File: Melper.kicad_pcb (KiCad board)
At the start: 2 copper layers, 160 x 60 mm, 41 parts, among them J1 Conn_01x02, J2 Conn_02x08_Odd_Even, J3 Conn_02x08_Odd_Even, J4 Conn_02x08_Odd_Even, J5 Conn_02x08_Odd_Even, J6 Conn_02x08_Odd_Even, U1 LM7805_TO220, U2 cui

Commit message: Version 2.1
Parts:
- removed C10, C11, C12, C13, C14, C15, C16, C17, C18, C19, C20, C21, C8, C9: .1uF, Capacitor_THT:C_Disc_D4.3mm_W1.9mm_P5.00mm
- C1: value .33uF -> 10uF; footprint Capacitor_THT:C_Disc_D4.3mm_W1.9mm_P5.00mm -> Capacitor_THT:CP_Radial_D8.0mm_P5.00mm
- C2: footprint Capacitor_THT:CP_Radial_Tantal_D5.0mm_P5.00mm -> Capacitor_THT:CP_Radial_D8.0mm_P5.00mm
- C5, C7: value .1uF -> 10uF; footprint Capacitor_THT:C_Disc_D4.3mm_W1.9mm_P5.00mm -> Capacitor_THT:CP_Radial_D8.0mm_P5.00mm
- C6: value 22uF -> 10uF; footprint Capacitor_THT:CP_Radial_Tantal_D6.0mm_P5.00mm -> Capacitor_THT:CP_Radial_D8.0mm_P5.00mm
- R1, R3: value 1K -> 10K
- R2: value 1K -> 4.7K
- U1: footprint Package_TO_SOT_THT:TO-220-3_Vertical -> Package_TO_SOT_THT:TO-220-3_Horizontal_TabDown
- U2: value cui -> VXO78012-1000
- moved J6 123.8 mm to (192.5, 88.3), turned to 180 degrees
- moved J2 89.2 mm to (72.5, 88.3), turned to 180 degrees
- moved U1 40.2 mm to (51.0, 47.8), turned to -90 degrees
- moved C4 38.6 mm to (45.1, 52.9), turned to -90 degrees
- moved C1 34.8 mm to (45.1, 47.8), turned to 90 degrees
- moved J5 32.7 mm to (162.5, 88.3), turned to 180 degrees
- moved C5 23.5 mm to (101.5, 43.9), turned to -90 degrees
- moved J3 18.0 mm to (102.5, 88.3), turned to 180 degrees
- moved J4 18.0 mm to (132.5, 88.3), turned to 180 degrees
- moved C6 16.4 mm to (101.5, 59.0), turned to 90 degrees
- moved C3 16.0 mm to (77.6, 47.8)
- moved L1 16.0 mm to (77.6, 52.8)
- moved U2 15.8 mm to (89.4, 52.8)
- moved C7 14.9 mm to (51.4, 78.1), turned to 90 degrees
- moved C2 14.4 mm to (88.0, 44.8), turned to 0 degrees
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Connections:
- C5 pad 1: -12V -> GND
- C5 pad 2: GND -> -12V
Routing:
- net +12V: track 0.00 -> 237.3 mm, vias 0 -> 2
- net -12V: track 185.7 -> 217.5 mm, vias 0 -> 2
- net Net-(D2-Pad2): track 9.13 -> 11.5 mm
- net Net-(D3-Pad2): track 6.44 -> 7.79 mm
- added copper zone on F.Cu, net GND
- removed copper zone on F.Cu, net +12V
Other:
- board text added: "-12V"
- board text added: "S/N 2.1."
- board text added: "v2.1"
- board text removed: "S/N 1.1."
- board text removed: "v1.1"

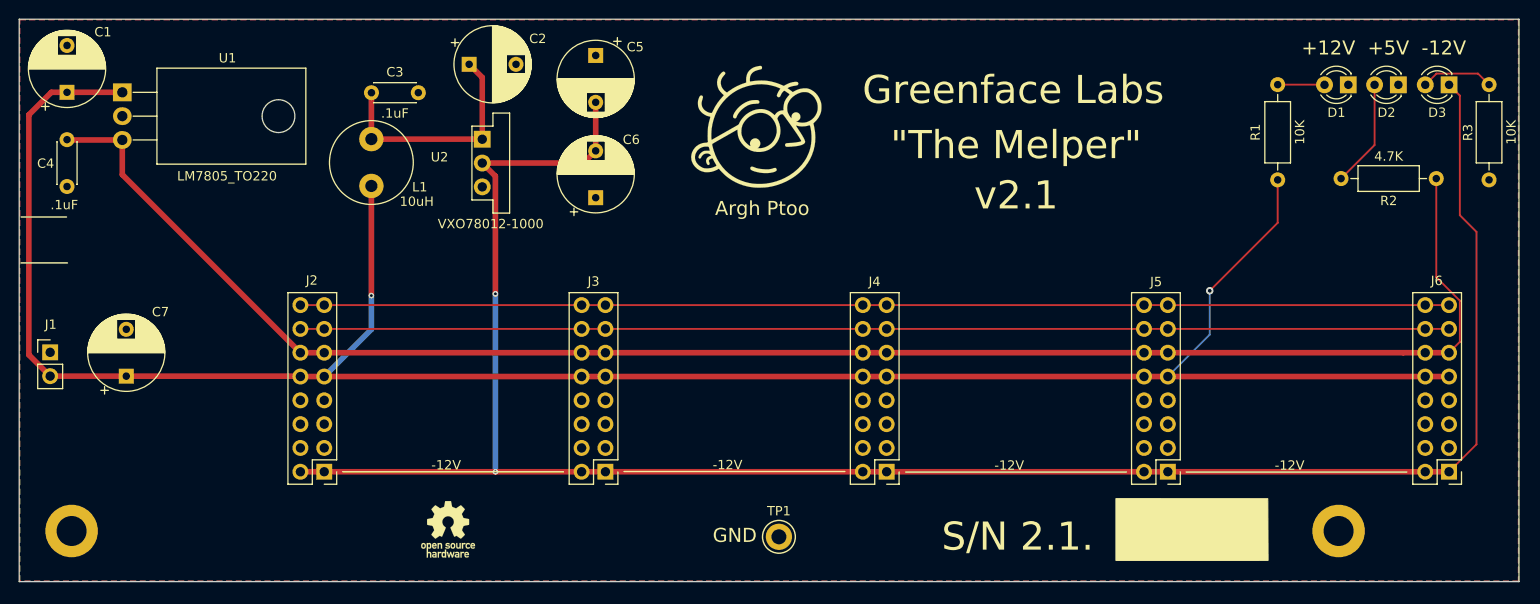
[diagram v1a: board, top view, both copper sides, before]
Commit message: Version 3
Adds 6th power connector.
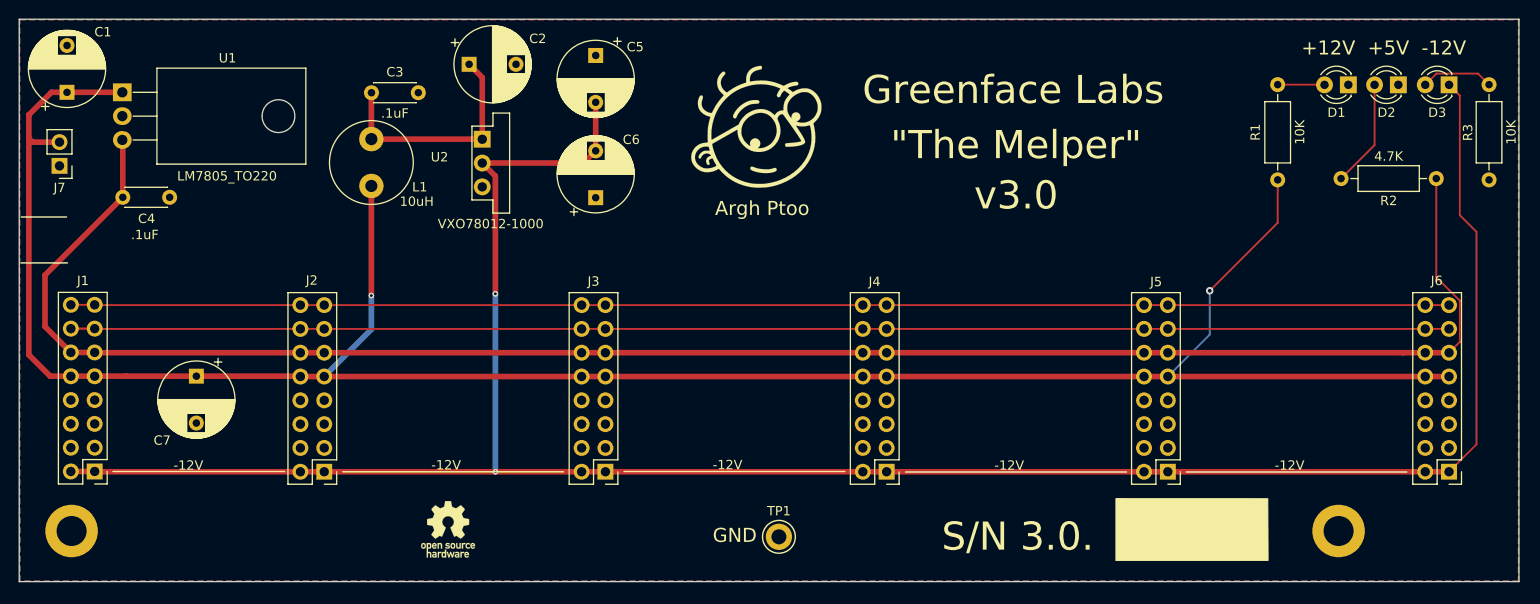
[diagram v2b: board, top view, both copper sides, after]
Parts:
- added J7: Conn_01x02, Connector_PinHeader_2.54mm:PinHeader_1x02_P2.54mm_Vertical, F.Cu at (44.3, 55.6)
- J1: value Conn_01x02 -> Conn_02x08_Odd_Even; footprint Connector_PinHeader_2.54mm:PinHeader_1x02_P2.54mm_Vertical -> Connector_PinHeader_2.54mm:PinHeader_2x08_P2.54mm_Vertical
- moved J1 13.6 mm to (48.0, 88.2), turned to 180 degrees
- moved C4 8.56 mm to (51.0, 59.0), turned to 0 degrees
- moved C7 7.48 mm to (58.9, 78.1), turned to -90 degrees
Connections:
- J1 pad 1: GND -> -12V
- J1 pad 2: +12V -> -12V
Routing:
- net CV: track 122.5 -> 147.0 mm
- net -12V: track 217.5 -> 242.0 mm
- net GATE: track 122.5 -> 147.0 mm
- net +5V: track 179.1 -> 194.4 mm
- net +12V: track 237.3 -> 240.7 mm
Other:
- board text added: "S/N 3.0."
- board text added: "v3.0"
- board text removed: "S/N 2.1."
- board text removed: "v2.1"

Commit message: Rev 3.2
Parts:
- added TP2: TestPoint, TestPoint:TestPoint_Pad_D2.0mm, F.Cu at (94.1, 95.2)
- added TP3: TestPoint, TestPoint:TestPoint_Pad_D2.0mm, F.Cu at (110.0, 95.2)
- added TP4: TestPoint, TestPoint:TestPoint_Pad_D2.0mm, F.Cu at (102.5, 95.2)
- moved H1 10.0 mm to (55.6, 95.6)
- moved GR2 5.00 mm to (80.8, 94.4)
- moved H2 1.00 mm to (180.8, 95.6)
- moved J7 0.98 mm to (44.1, 56.6), turned to 0 degrees
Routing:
- net +5V: track 194.4 -> 217.2 mm, vias 0 -> 1
- net +12V: track 240.7 -> 259.9 mm, vias 2 -> 3
- net -12V: track 242.0 -> 249.0 mm, vias 2 -> 3
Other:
- board text added: "+12"
- board text added: "+12V"
- board text added: "+5V"
- board text added: "S/N 3.2."
- board text added: "v3.2"
- board text removed: "S/N 3.0."
- board text removed: "v3.0"

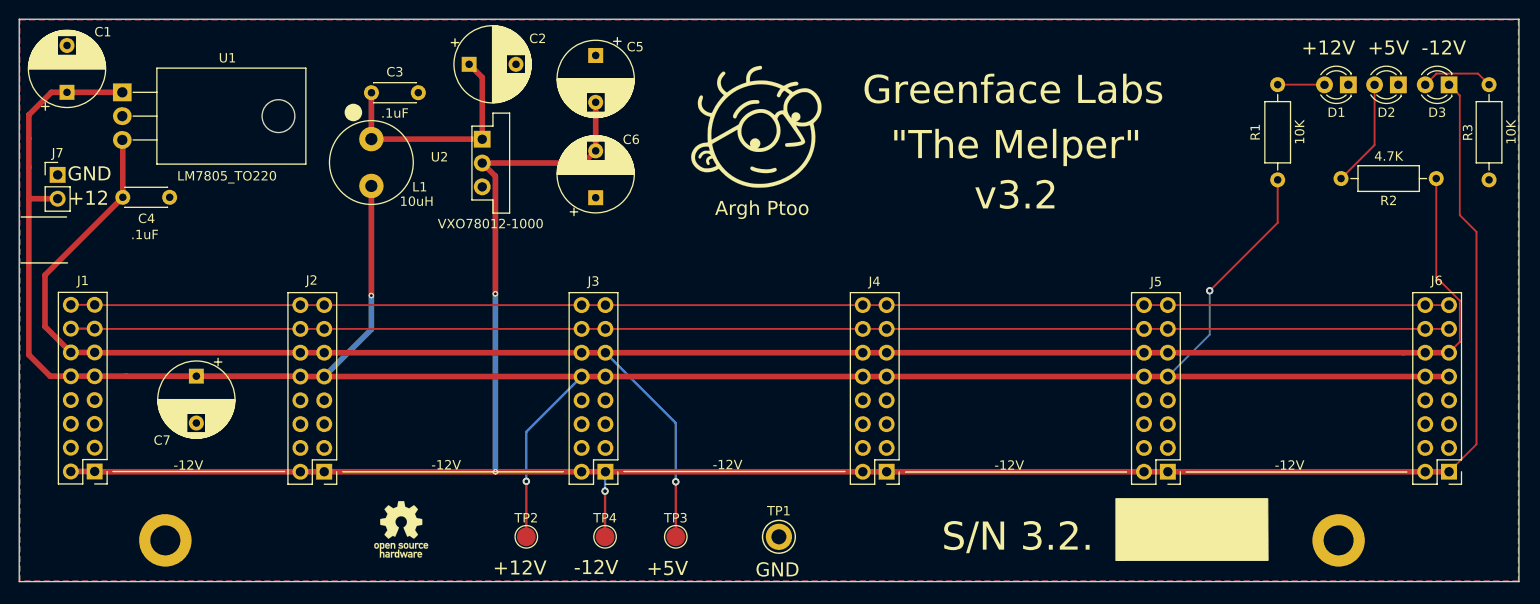
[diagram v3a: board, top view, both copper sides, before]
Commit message: Revision 3.5
Changes negative regulator.
Adds support for JLC build.
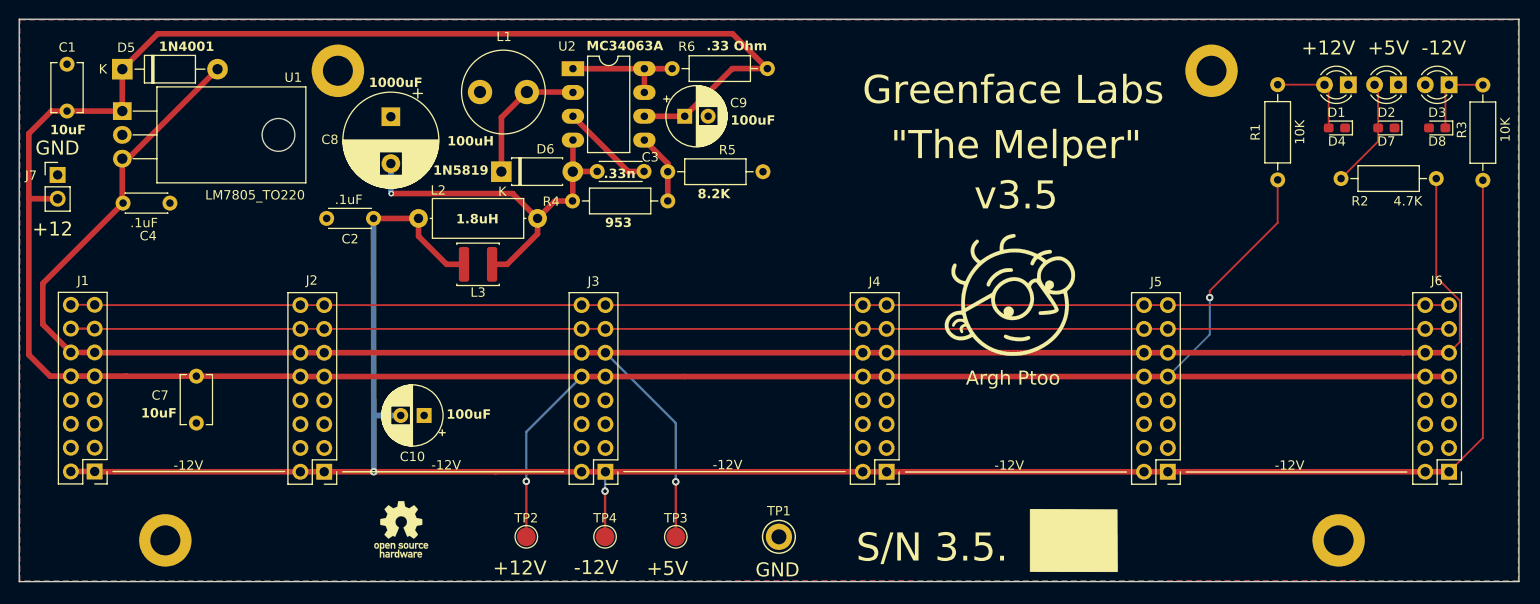
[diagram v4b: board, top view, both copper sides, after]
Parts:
- removed C5, C6: 10uF, Capacitor_THT:CP_Radial_D8.0mm_P5.00mm
- added C10: 100uF, Capacitor_THT:CP_Radial_D6.3mm_P2.50mm, F.Cu at (83.2, 82.3)
- added C8: 1000uF, Capacitor_THT:CP_Radial_D10.0mm_P5.00mm, F.Cu at (79.7, 50.4)
- added C9: 100uF, Capacitor_THT:CP_Radial_D6.3mm_P2.50mm, F.Cu at (111.0, 50.4)
- added D4: Red SMT LED, LED_SMD:LED_0603_1608Metric_Pad1.05x0.95mm_HandSolder, F.Cu at (180.6, 51.6)
- added D5: 1N4001, Diode_THT:D_DO-41_SOD81_P10.16mm_Horizontal, F.Cu at (51.0, 45.3)
- added D6: 1N5819, Diode_THT:D_DO-41_SOD81_P7.62mm_Horizontal, F.Cu at (91.4, 56.3)
- added D7: Yellow LED, LED_SMD:LED_0603_1608Metric_Pad1.05x0.95mm_HandSolder, F.Cu at (185.8, 51.6)
- added D8: Blue SMT LED, LED_SMD:LED_0603_1608Metric_Pad1.05x0.95mm_HandSolder, F.Cu at (191.3, 51.6)
- added H3: MountingHole_Pad, MountingHole:MountingHole_3.2mm_M3_DIN965_Pad, F.Cu at (74.0, 45.5)
- added H4: MountingHole_Pad, MountingHole:MountingHole_3.2mm_M3_DIN965_Pad, F.Cu at (167.2, 45.5)
- added L2: 1.8uH, Inductor_THT:L_Axial_L9.5mm_D4.0mm_P12.70mm_Horizontal_Fastron_SMCC, F.Cu at (95.3, 61.2)
- added L3: 1.8uH, Inductor_SMD:L_Sunlord_SWPA4012S, F.Cu at (89.0, 66.2)
- added R4: 953, Resistor_THT:R_Axial_DIN0207_L6.3mm_D2.5mm_P10.16mm_Horizontal, F.Cu at (99.0, 59.4)
- added R5: 8.2K, Resistor_THT:R_Axial_DIN0207_L6.3mm_D2.5mm_P10.16mm_Horizontal, F.Cu at (119.3, 56.3)
- added R6: .33, Resistor_THT:R_Axial_DIN0207_L6.3mm_D2.5mm_P10.16mm_Horizontal, F.Cu at (119.8, 45.3)
- C1, C7: footprint Capacitor_THT:CP_Radial_D8.0mm_P5.00mm -> Capacitor_THT:C_Disc_D5.1mm_W3.2mm_P5.00mm
- C2: value 10uF -> .1uF; footprint Capacitor_THT:CP_Radial_D8.0mm_P5.00mm -> Capacitor_THT:C_Disc_D4.3mm_W1.9mm_P5.00mm
- C3: value .1uF -> 330pF
- L1: value 10uH -> 100uH
- U2: value VXO78012-1000 -> MC34063AD; footprint Converter_DCDC:Converter_DCDC_Murata_OKI-78SR_Vertical -> Package_DIP:DIP-8_W7.62mm_LongPads
- moved GR1 32.5 mm to (145.6, 69.8)
- moved C3 30.3 mm to (106.7, 56.2), turned to 180 degrees
- moved C2 19.3 mm to (77.8, 61.2), turned to 180 degrees
- moved L1 17.3 mm to (94.2, 47.8), turned to 180 degrees
- moved U2 12.3 mm to (99.1, 45.3), turned to 0 degrees
- moved R3 10.1 mm to (196.2, 47.0), turned to -90 degrees
- moved C1 2.00 mm to (45.1, 49.8)
- moved U1 2.00 mm to (51.0, 49.8)
- moved C4 0.62 mm to (51.1, 59.6)
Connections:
- C2 pad 1: Net-(C2-Pad1) -> -12V
- C3 pad 1: Net-(C2-Pad1) -> Net-(U2-TC)
- C3 pad 2: GND -> Net-(D6-A)
- D3 pad 1: -12V -> Net-(D3-K)
- D3 pad 2: Net-(D3-Pad2) -> GND
- L1 pad 1: Net-(C2-Pad1) -> Net-(D6-K)
- L1 pad 2: +12V -> GND
- R3 pad 1: GND -> Net-(D3-K)
- R3 pad 2: Net-(D3-Pad2) -> -12V
- U2 pad 1: Net-(C2-Pad1) -> Net-(U2-DC)
- U2 pad 2: -12V -> Net-(D6-K)
- U2 pad 3: GND -> Net-(U2-TC)
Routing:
- net +12V: track 259.9 -> 327.1 mm, vias 3 -> 2
- net Net-(D6-A): track 0.00 -> 41.4 mm, vias 0 -> 1
- net Net-(C2-Pad1): track 25.4 -> 0.00 mm
- net -12V: track 249.0 -> 229.3 mm, vias 3 -> 2
- net Net-(D6-K): track 0.00 -> 14.6 mm
- net Net-(U2-DC): track 0.00 -> 13.1 mm
- net +5V: track 217.2 -> 229.6 mm
- net Net-(U2-TC): track 0.00 -> 10.0 mm
- net Net-(D3-K): track 0.00 -> 8.38 mm
- net Net-(D3-Pad2): track 7.79 -> 0.00 mm
- net Net-(U2-Vfb): track 0.00 -> 7.54 mm
- net Net-(D1-A): track 5.00 -> 9.79 mm
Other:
- board text added: ".1uF"
- board text added: ".33 Ohm"
- board text added: ".33n"
- board text added: "1.8uH"
- board text added: "1000uF"
- board text added: "100uF"
- board text added: "100uH"
- board text added: "10uF"
- board text added: "1N4001"
- board text added: "1N5819"
- board text added: "8.2K"
- board text added: "953"
- board text added: "MC34063A"
- board text added: "S/N 3.5."
- board text added: "v3.5"
- board text removed: "S/N 3.2."
- board text removed: "v3.2"
